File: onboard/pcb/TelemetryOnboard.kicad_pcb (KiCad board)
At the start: 4 copper layers, 95 x 95 mm, 147 parts, among them J1 USB-C, J2 USB-C, J3 CONSMA001-SMD-G-T, J4 CONSMA001-SMD-G-T, M1 M4 Mounting Hole, M2 M4 Mounting Hole, M3 M4 Mounting Hole, M4 M4 Mounting Hole, Q1 NPN, U1 CP2102N, U2 CP2102N, U3 RC1780HP-RC232, U4 RC1701HP-RC232, U5 AVR128DB64x-xPT, U6 W25Q80DVSSIG

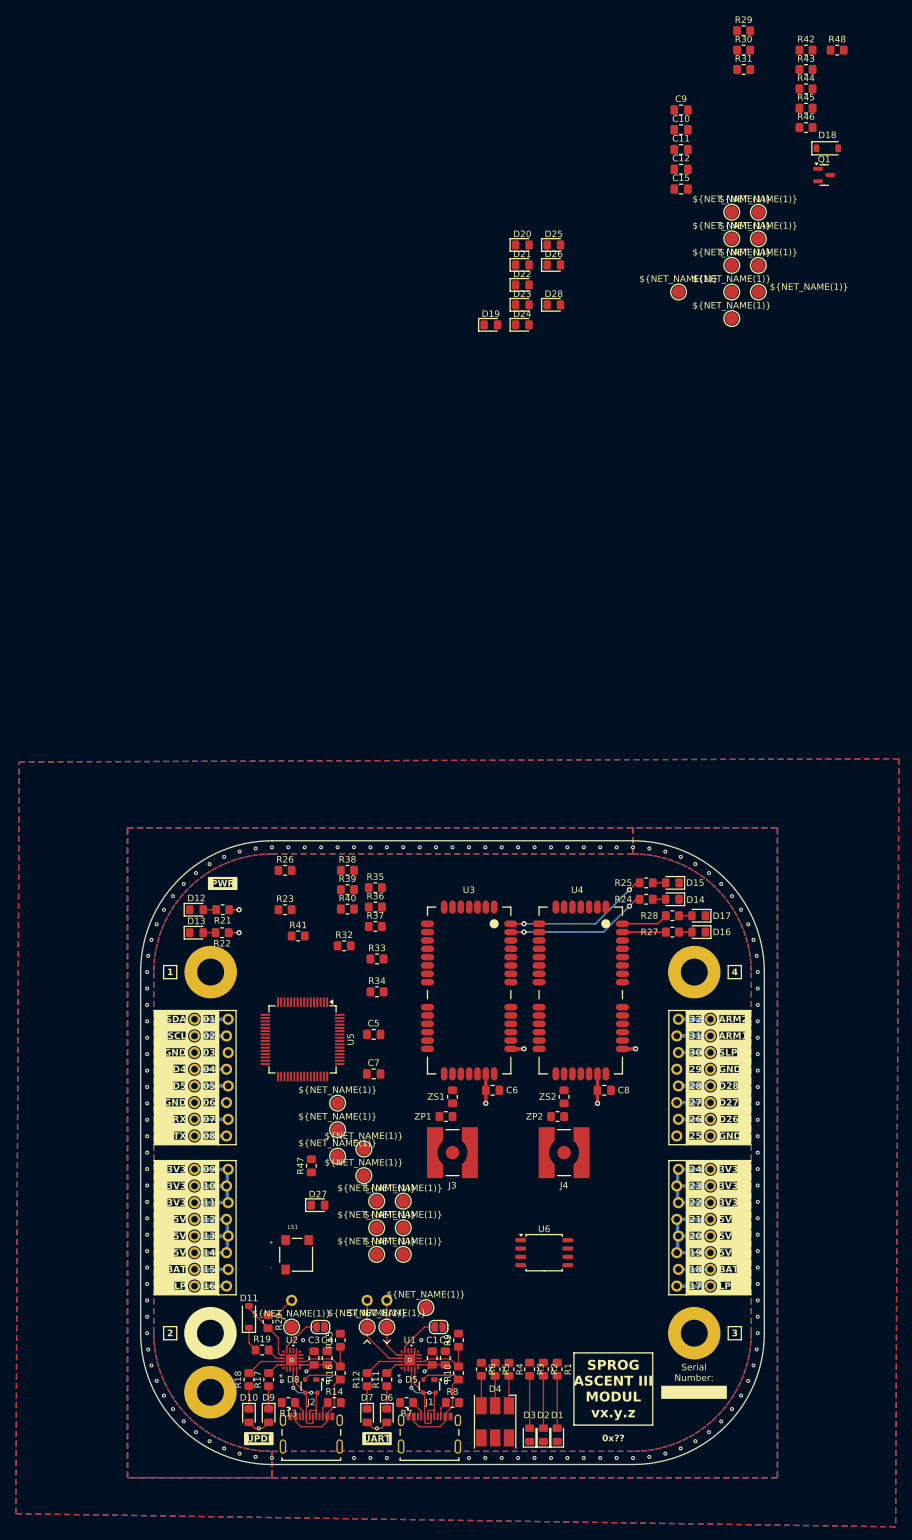
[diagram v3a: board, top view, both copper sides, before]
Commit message: clean up schematic and add tht sma conn
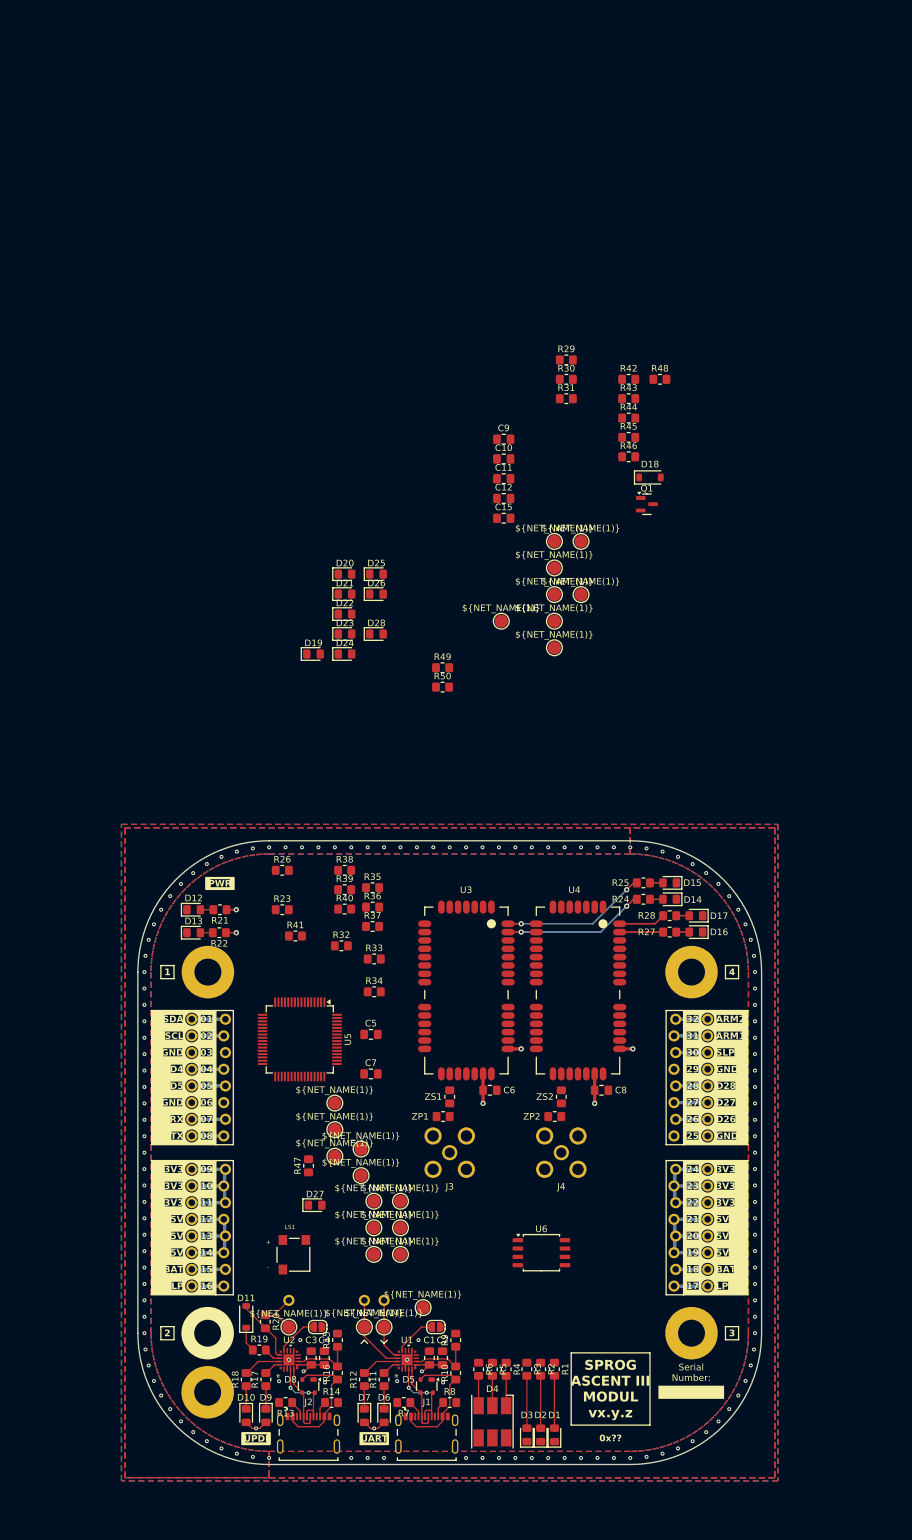
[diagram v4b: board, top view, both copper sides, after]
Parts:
- removed TP40, TP42: ~, Footprints:Test Point
- added R49: 5k6, Resistor_SMD:R_0805_2012Metric_Pad1.20x1.40mm_HandSolder, F.Cu at (-1.09, -73.9)
- added R50: 5k6, Resistor_SMD:R_0805_2012Metric_Pad1.20x1.40mm_HandSolder, F.Cu at (-1.09, -70.9)
- C10, C11, C12, C9: value 0805 1uF -> 1 uF
- C5, C7: value 0805 1nF -> 1 nF
- D14, D16: value LED 0805 green -> green
- D15, D17: value LED 0805 yellow -> yellow
- D19, D20, D21, D22, D23, D24: value LED 0805 red -> red
- D25, D26, D27, D28: value LED 0805 orange -> orange
- J3, J4: value CONSMA001-SMD-G-T -> RFPC-SMA28-F; footprint Footprints:SMA Connector CONSMA001-SMD-G-T -> Footprints:RFPC-SMA28-F; moved to B.Cu
- R23, R26: value 0805 2k7 -> 2k7
- R24, R25, R27, R28: value 0805 270R -> 560R
- R30, R31: value 10kR -> 5k6
- R32, R33, R35, R36, R43, R44: value 0805 1k -> 1k
- R34, R37, R38, R39, R40, R41: value 0805 5k6 -> 5k6
- R42: value 5.6kR -> 5k6
- R45, R46, R47, R48: value 0805 270R -> 270R
- TP16, TP17, TP70, TP80: value ~ -> TestPoint
- moved C10 57.0 mm to (8.23, -105.7)
- moved C15 57.0 mm to (8.23, -96.6)
- moved D22 57.0 mm to (-15.9, -82.0)
- moved R45 57.0 mm to (27.3, -108.9)
- moved TP18 57.0 mm to (15.9, -93.1)
- moved TP39 57.0 mm to (20.0, -93.1)
- moved C12 57.0 mm to (8.23, -99.6)
- moved C9 57.0 mm to (8.23, -108.7)
- moved D19 57.0 mm to (-20.7, -76.0)
- moved D20 57.0 mm to (-15.9, -88.1)
- moved D21 57.0 mm to (-15.9, -85.1)
- moved D24 57.0 mm to (-15.9, -76.0)
- moved D25 57.0 mm to (-11.2, -88.1)
- moved D26 57.0 mm to (-11.2, -85.1)
- moved Q1 57.0 mm to (30.0, -98.8)
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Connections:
- net Net-(U5-PB1) renamed BUZZ
- R31 pad 1: +3V3 -> SDA1
- R31 pad 2: SDA1 -> +3V3
- R34 pad 1: +3V3 -> TX0
- R34 pad 2: TX0 -> +3V3
- R37 pad 1: +3V3 -> TX1
- R37 pad 2: TX1 -> +3V3
- R38 pad 1: +3V3 -> RST1
- R38 pad 2: RST1 -> +3V3
- R39 pad 1: +3V3 -> RST2
- R39 pad 2: RST2 -> +3V3
- R40 pad 1: +3V3 -> CFG2
- R40 pad 2: CFG2 -> +3V3
- R41 pad 1: +3V3 -> CFG1
- R41 pad 2: CFG1 -> +3V3

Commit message: change usb connector and add tvs diode
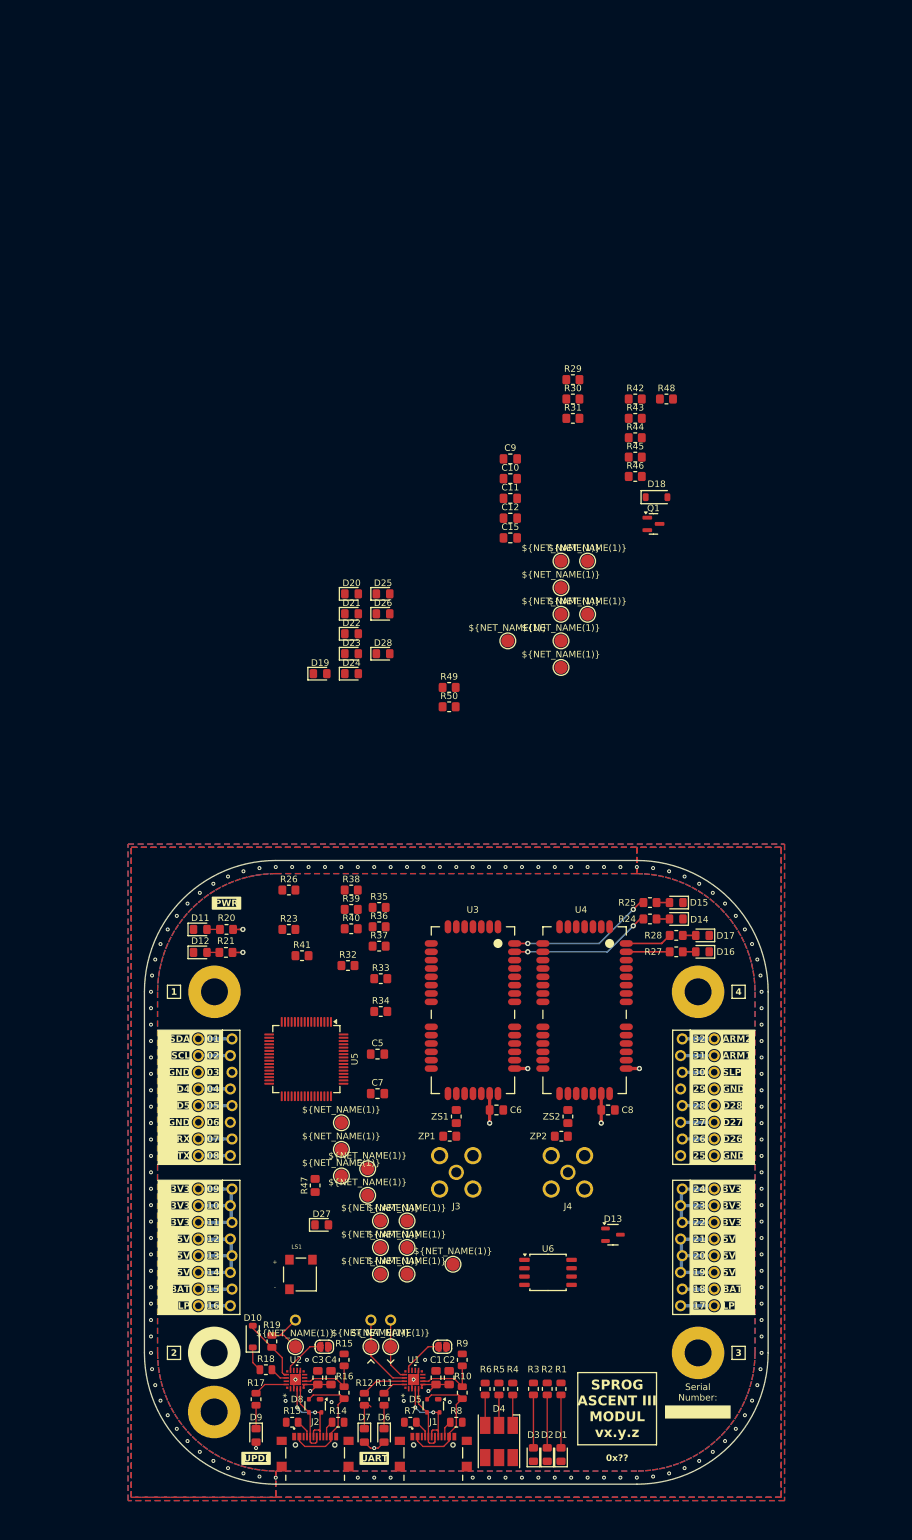
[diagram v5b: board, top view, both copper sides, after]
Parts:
- removed the D11 at (-31.0, 25.0)
- removed the R20 at (-28.1, 25.8)
- removed the REF** at (-24.5, 22.5)
- removed the REF** at (-10.0, 22.5)
- removed the REF** at (-13.0, 22.5)
- added D13: WE-TVS_SOT23-3L_824021, Package_TO_SOT_SMD:SOT-23-3, F.Cu at (24.9, 12.5)
- added REF**: Test Point Hole, Footprints:Test Point Hole, F.Cu at (-9.00, 25.5)
- added REF**: Test Point Hole, Footprints:Test Point Hole, F.Cu at (-23.5, 25.5)
- added REF**: Test Point Hole, Footprints:Test Point Hole, F.Cu at (-12.0, 25.5)
- D10: value orange -> BAT43; footprint LED_SMD:LED_0805_2012Metric_Pad1.15x1.40mm_HandSolder -> Diode_SMD:D_SOD-123
- D9: value green -> red
- J1, J2: footprint Footprints:GCT_USB4215-03-A_REVA -> Footprints:GCT_USB4216-03-A_REVA
- R1, R10, R11, R12, R13, R14, R15, R16, R17, R19, R2, R3, R4, R5, R6, R7, R8, R9: footprint Resistor_SMD:R_0805_2012Metric_Pad1.20x1.40mm_HandSolder -> Resistor_SMD:R_0805_2012Metric
- R18: value 560 Ohm -> 470 Ohm; footprint Resistor_SMD:R_0805_2012Metric_Pad1.20x1.40mm_HandSolder -> Resistor_SMD:R_0805_2012Metric
- moved D10 12.1 mm to (-30.0, 28.0), turned to 90 degrees
- moved TP12 8.02 mm to (0.50, 17.0)
- moved D9 3.35 mm to (-29.5, 43.1)
- moved R17 3.35 mm to (-29.5, 37.6)
- moved R18 3.35 mm to (-28.0, 33.1), turned to 0 degrees
- moved D16 3.16 mm to (38.5, -30.6)
- moved R27 3.16 mm to (34.5, -30.6)
- moved R37 3.16 mm to (-10.8, -31.4)
- moved C5 3.16 mm to (-11.0, -15.0)
- moved LS1 3.16 mm to (-22.8, 18.6)
- moved C10 3.16 mm to (9.23, -102.7)
- moved C11 3.16 mm to (9.23, -99.7)
- moved C12 3.16 mm to (9.23, -96.6)
- moved C15 3.16 mm to (9.23, -93.6)
- moved C6 3.16 mm to (7.12, -6.50)
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- renumbered D12 to D11, D13 to D12, R21 to R20, R22 to R21
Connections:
- D10 pad 2: +3V3 -> Net-(D10-A)
- R18 pad 2: Net-(U2-~{RXT}/GPIO.3) -> Net-(U2-TXD)
- R19 pad 1: Net-(D11-K) -> UPDI
- R19 pad 2: Net-(U2-TXD) -> Net-(D10-A)
- U2 pad 17: Net-(D11-A) (its old number) -> Net-(D10-A)
- U2 pad 19: Net-(U2-~{RXT}/GPIO.3) -> unconnected-(U2-~{RXT}/GPIO.3-Pad19)
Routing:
- net Net-(D11-A) (its old number): track 10.1 -> 0.00 mm
- net Net-(D10-A): track 0.00 -> 10.1 mm
- net Net-(U2-~{RXT}/GPIO.3): track 5.86 -> 0.00 mm
- net Net-(D11-K): track 3.85 -> 0.00 mm
- net +3V3: track 70.4 -> 67.6 mm
- net Net-(U2-~{TXT}/GPIO.2): track 2.66 -> 5.16 mm
- net Net-(U1-~{RXT}/GPIO.3): track 5.86 -> 6.86 mm
- net Net-(U1-~{TXT}/GPIO.2): track 2.66 -> 3.66 mm
